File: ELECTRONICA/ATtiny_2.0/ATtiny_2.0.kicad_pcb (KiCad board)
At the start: 2 copper layers, 77.4 x 127.8 mm, 148 parts, among them J1 Puerto_Temperatura_1, J10 Agujero2, J11 Agujero3, J12 Agujero4, J13 GND, J14 VCC, J15 XT30, J2 Puerto_Temperatura_2, J3 I2C0, J4 I2C1, J5 Puerto Motores, J6 UART0, J7 Puerto_Encoders, J8 ICSP, J9 Agujero1, SW1 SW_Push, SW2 SW_DIP_x04, U1 ATtiny1634-SU, U2 L7805, Y1 Crystal 16MHz

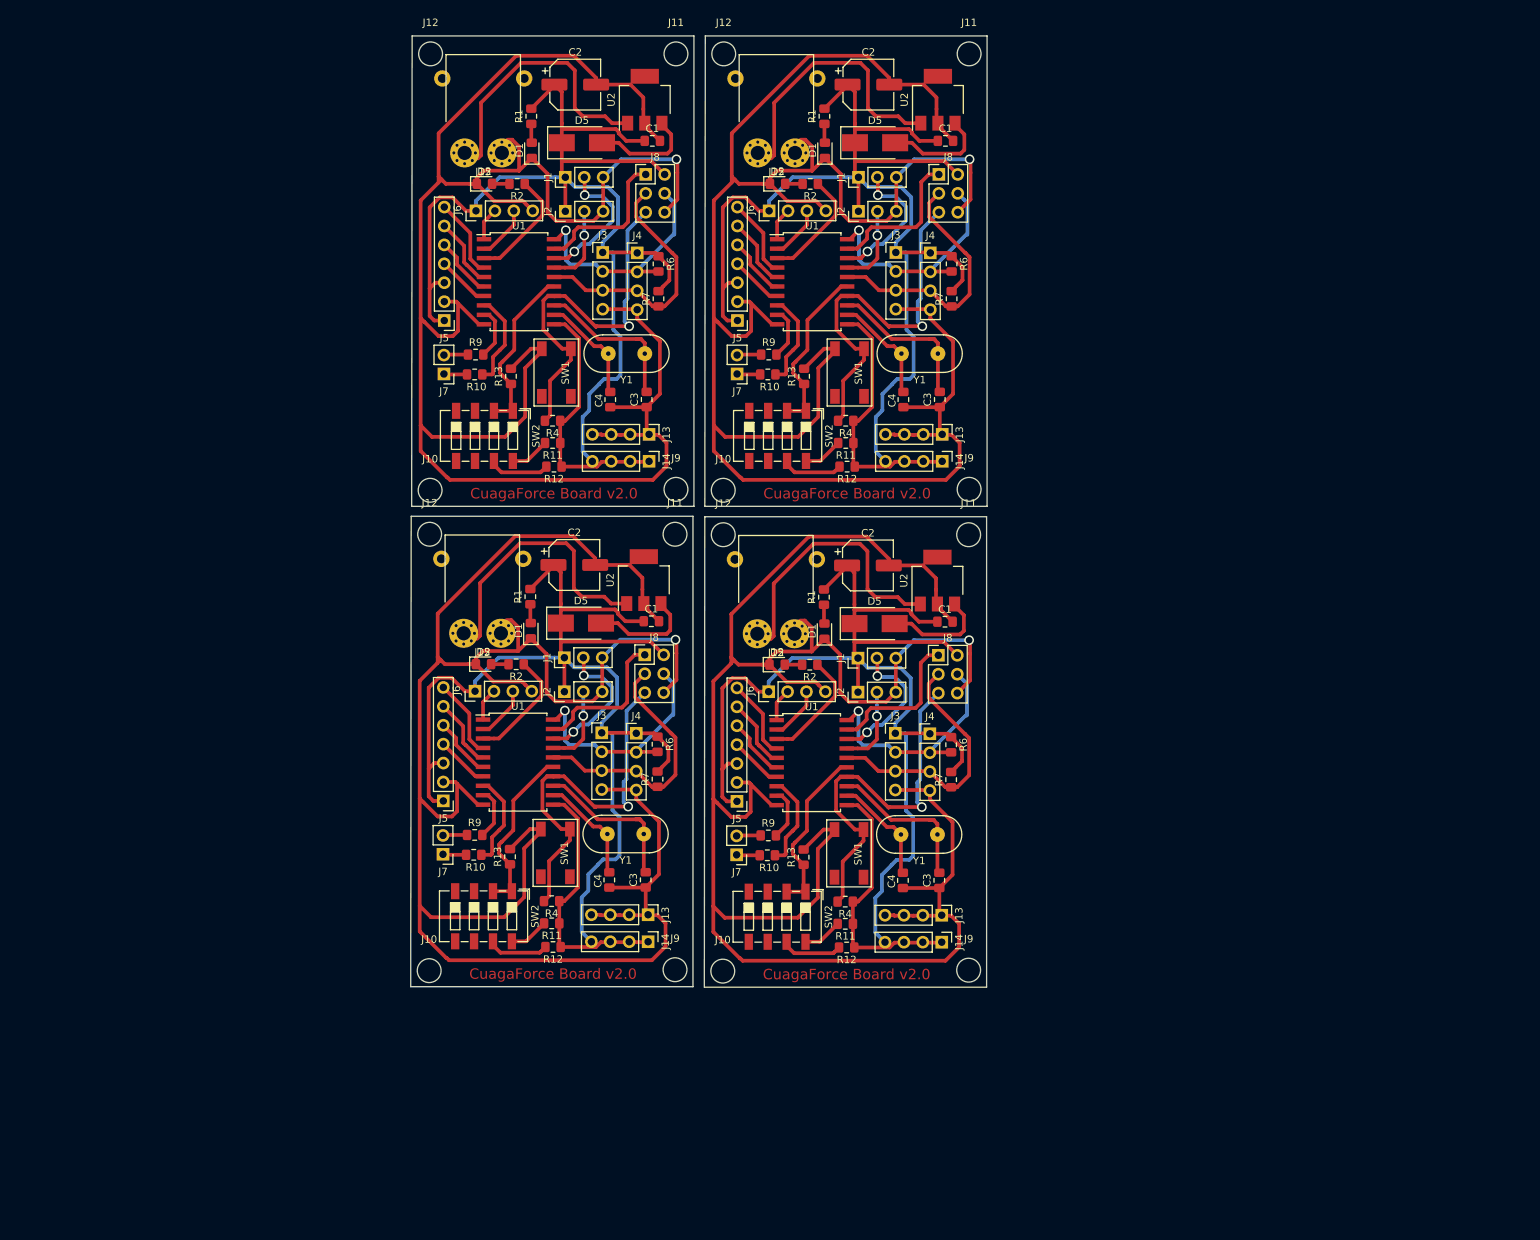
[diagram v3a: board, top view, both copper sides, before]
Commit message: controller reader and controller tanformer to pollotron robot
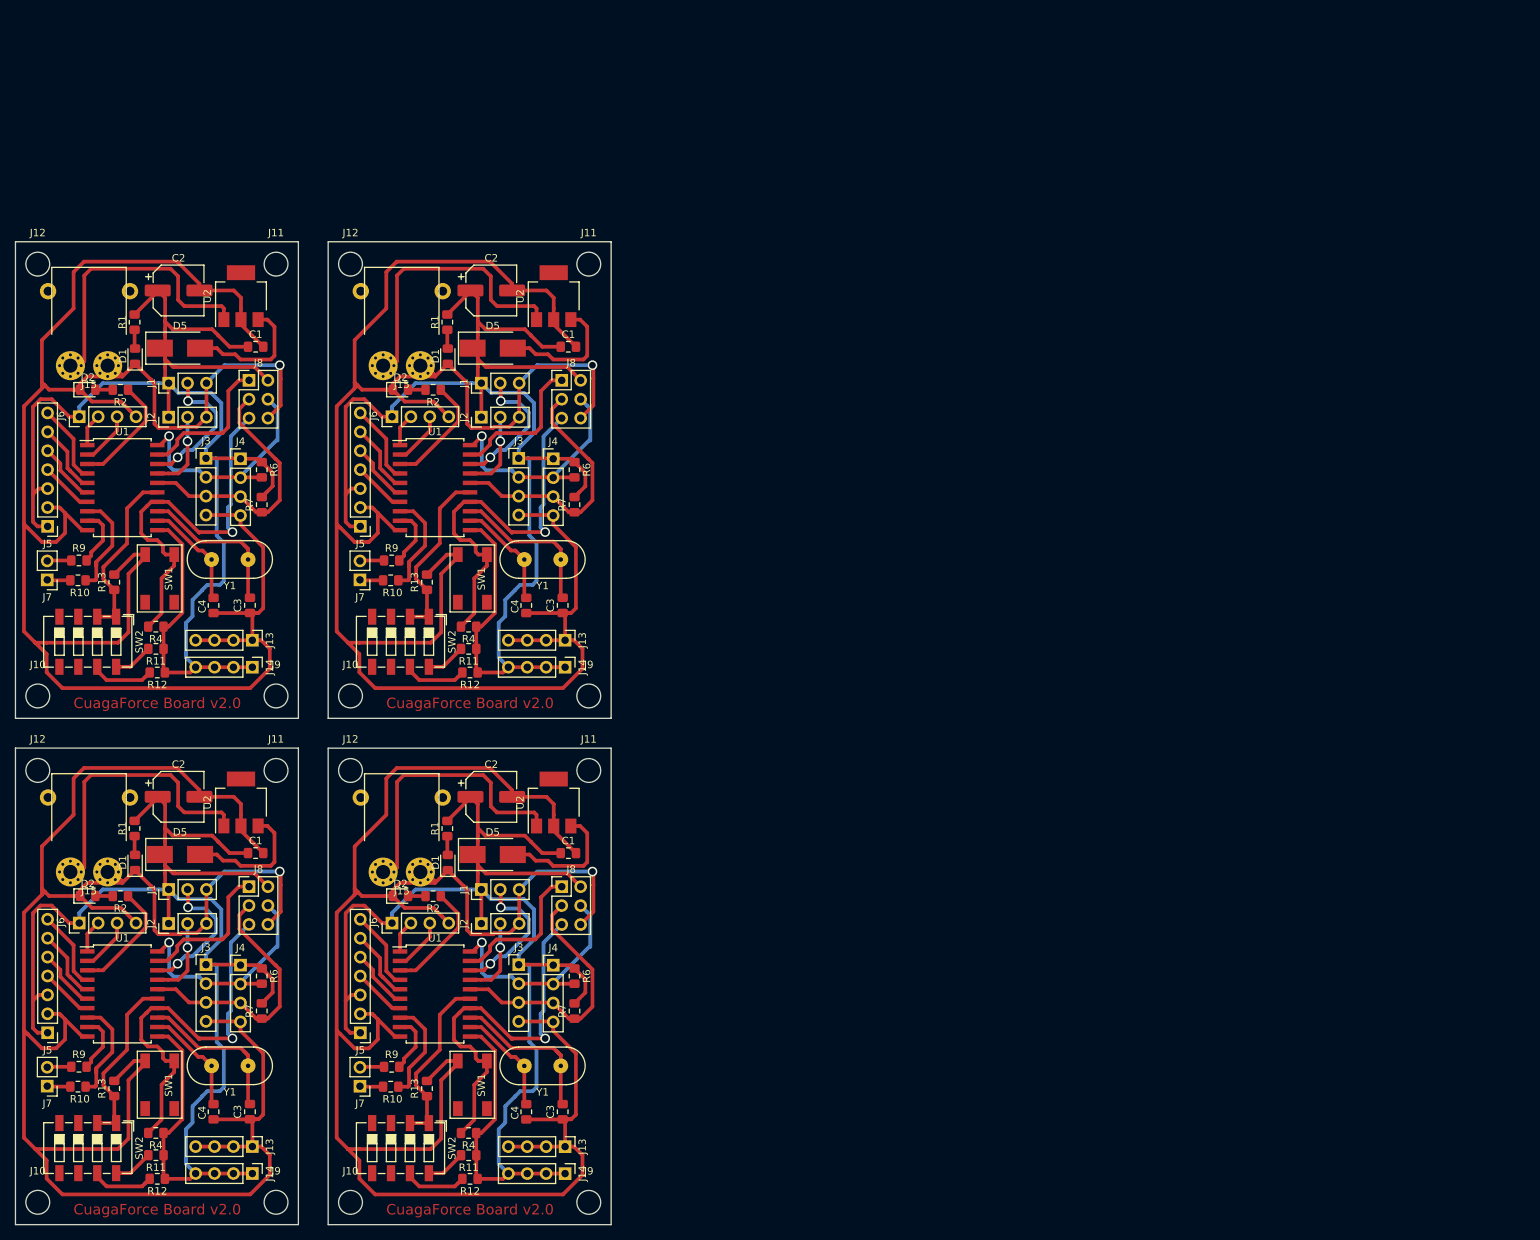
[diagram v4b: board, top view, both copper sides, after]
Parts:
- removed the C1 at (136.8, 89.0)
- removed the C1 at (97.4, 89.0)
- removed the C1 at (136.9, 24.4)
- removed the C2 at (126.5, 81.5)
- removed the C2 at (87.1, 81.4)
- removed the C2 at (126.6, 16.9)
- removed the C3 at (136.1, 123.8)
- removed the C3 at (96.6, 123.7)
- removed the C3 at (136.1, 59.2)
- removed the C4 at (131.2, 123.8)
- removed the C4 at (91.8, 123.7)
- removed the C4 at (131.3, 59.2)
- removed the D1 at (120.7, 90.3)
- removed the D1 at (81.2, 90.2)
- removed the D1 at (120.7, 25.7)
- removed the D2 at (114.3, 94.8)
- removed the D2 at (74.9, 94.7)
- removed the D2 at (114.4, 30.2)
- removed the D5 at (127.4, 89.3)
- removed the D5 at (87.9, 89.2)
- removed the D5 at (127.4, 24.7)
- removed the J1 at (125.2, 93.9)
- removed the J1 at (85.7, 93.9)
- removed the J1 at (125.2, 29.3)
- removed the J10 at (107.0, 136.0)
- removed the J10 at (67.6, 135.9)
- removed the J10 at (107.1, 71.4)
- removed the J11 at (140.0, 77.3)
- removed the J11 at (100.6, 77.3)
- removed the J11 at (140.1, 12.8)
- removed the J12 at (107.1, 77.3)
- removed the J12 at (67.6, 77.3)
- removed the J12 at (107.1, 12.8)
- removed the J13 at (136.4, 128.4)
- removed the J13 at (97.0, 128.4)
- removed the J13 at (136.5, 63.9)
- removed the J14 at (136.4, 132.1)
- removed the J14 at (97.0, 132.0)
- removed the J14 at (136.5, 67.5)
- removed the J15 at (114.1, 90.6)
- removed the J15 at (74.7, 90.6)
- removed the J15 at (114.2, 26.1)
- removed the J2 at (125.2, 98.5)
- removed the J2 at (85.7, 98.4)
- removed the J2 at (125.2, 33.9)
- removed the J3 at (130.2, 104.0)
- removed the J3 at (90.7, 103.9)
- removed the J3 at (130.2, 39.4)
- removed the J4 at (134.8, 104.1)
- removed the J4 at (95.4, 104.0)
- removed the J4 at (134.9, 39.5)
- removed the J5 at (108.9, 113.2)
- removed the J5 at (69.5, 113.1)
- removed the J5 at (109.0, 48.6)
- removed the J6 at (113.2, 98.4)
- removed the J6 at (73.7, 98.4)
- removed the J6 at (113.2, 33.8)
- removed the J7 at (108.9, 120.3)
- removed the J7 at (69.4, 120.3)
- removed the J7 at (108.9, 55.8)
- removed the J8 at (136.0, 93.5)
- removed the J8 at (96.5, 93.5)
- removed the J8 at (136.0, 29.0)
- removed the J9 at (140.0, 135.8)
- removed the J9 at (100.6, 135.8)
- removed the J9 at (140.1, 71.2)
- removed the R1 at (120.6, 85.7)
- removed the R1 at (81.2, 85.7)
- removed the R1 at (120.7, 21.1)
- removed the R10 at (113.0, 120.4)
- removed the R10 at (73.5, 120.3)
- removed the R10 at (113.0, 55.8)
- removed the R11 at (123.5, 129.6)
- removed the R11 at (84.0, 129.5)
- removed the R11 at (123.5, 65.0)
- removed the R12 at (123.6, 132.8)
- removed the R12 at (84.2, 132.7)
- removed the R12 at (123.7, 68.2)
- removed the R13 at (117.9, 120.7)
- removed the R13 at (78.4, 120.6)
- removed the R13 at (117.9, 56.1)
- removed the R2 at (118.7, 94.8)
- removed the R2 at (79.2, 94.7)
- removed the R2 at (118.7, 30.2)
- removed the R4 at (123.4, 126.6)
- removed the R4 at (84.0, 126.6)
- removed the R4 at (123.5, 62.0)
- removed the R6 at (137.7, 105.5)
- removed the R6 at (98.2, 105.5)
- removed the R6 at (137.7, 41.0)
- removed the R7 at (137.7, 110.2)
- removed the R7 at (98.2, 110.2)
- removed the R7 at (137.7, 45.7)
- removed the R9 at (113.1, 117.7)
- removed the R9 at (73.7, 117.7)
- removed the R9 at (113.2, 53.2)
- removed the SW1 at (124.0, 120.1)
- removed the SW1 at (84.5, 120.1)
- removed the SW1 at (124.0, 55.6)
- removed the SW2 at (114.3, 128.7)
- removed the SW2 at (74.9, 128.6)
- removed the SW2 at (114.4, 64.1)
- removed the U1 at (118.9, 108.0)
- removed the U1 at (79.5, 107.9)
- removed the U1 at (119.0, 43.4)
- removed the U2 at (135.8, 83.5)
- removed the U2 at (96.4, 83.4)
- removed the U2 at (135.9, 18.9)
- removed the Y1 at (135.8, 117.6)
- removed the Y1 at (96.4, 117.5)
- removed the Y1 at (135.9, 53.0)
- added C1: C100nF, Capacitor_SMD:C_0805_2012Metric_Pad1.15x1.40mm_HandSolder, F.Cu at (86.3, 120.1)
- added C1: C100nF, Capacitor_SMD:C_0805_2012Metric_Pad1.15x1.40mm_HandSolder, F.Cu at (44.3, 120.1)
- added C1: C100nF, Capacitor_SMD:C_0805_2012Metric_Pad1.15x1.40mm_HandSolder, F.Cu at (86.3, 52.1)
- added C2: CP47uF, Capacitor_SMD:CP_Elec_6.3x5.3, F.Cu at (75.9, 112.5)
- added C2: CP47uF, Capacitor_SMD:CP_Elec_6.3x5.3, F.Cu at (33.9, 112.5)
- added C2: CP47uF, Capacitor_SMD:CP_Elec_6.3x5.3, F.Cu at (75.9, 44.5)
- added C3: C22pF, Capacitor_SMD:C_0805_2012Metric_Pad1.15x1.40mm_HandSolder, F.Cu at (85.5, 154.8)
- added C3: C22pF, Capacitor_SMD:C_0805_2012Metric_Pad1.15x1.40mm_HandSolder, F.Cu at (43.5, 154.8)
- added C3: C22pF, Capacitor_SMD:C_0805_2012Metric_Pad1.15x1.40mm_HandSolder, F.Cu at (85.5, 86.8)
- added C4: C22pF, Capacitor_SMD:C_0805_2012Metric_Pad1.15x1.40mm_HandSolder, F.Cu at (80.6, 154.8)
- added C4: C22pF, Capacitor_SMD:C_0805_2012Metric_Pad1.15x1.40mm_HandSolder, F.Cu at (38.6, 154.8)
- added C4: C22pF, Capacitor_SMD:C_0805_2012Metric_Pad1.15x1.40mm_HandSolder, F.Cu at (80.6, 86.8)
- added D1: LED, LED_SMD:LED_0805_2012Metric_Pad1.15x1.40mm_HandSolder, F.Cu at (70.1, 121.4)
- added D1: LED, LED_SMD:LED_0805_2012Metric_Pad1.15x1.40mm_HandSolder, F.Cu at (28.1, 121.4)
- added D1: LED, LED_SMD:LED_0805_2012Metric_Pad1.15x1.40mm_HandSolder, F.Cu at (70.1, 53.4)
- added D2: LED, LED_SMD:LED_0805_2012Metric_Pad1.15x1.40mm_HandSolder, F.Cu at (63.7, 125.9)
- added D2: LED, LED_SMD:LED_0805_2012Metric_Pad1.15x1.40mm_HandSolder, F.Cu at (21.7, 125.9)
- added D2: LED, LED_SMD:LED_0805_2012Metric_Pad1.15x1.40mm_HandSolder, F.Cu at (63.7, 57.9)
- added D5: US2D, Diode_SMD:D_SMB_Handsoldering, F.Cu at (76.1, 120.3)
- added D5: US2D, Diode_SMD:D_SMB_Handsoldering, F.Cu at (34.1, 120.3)
- added D5: US2D, Diode_SMD:D_SMB_Handsoldering, F.Cu at (76.1, 52.3)
- added J1: Puerto_Temperatura_1, Connector_PinHeader_2.54mm:PinHeader_1x03_P2.54mm_Vertical, F.Cu at (74.6, 125.0)
- added J1: Puerto_Temperatura_1, Connector_PinHeader_2.54mm:PinHeader_1x03_P2.54mm_Vertical, F.Cu at (32.6, 125.0)
- added J1: Puerto_Temperatura_1, Connector_PinHeader_2.54mm:PinHeader_1x03_P2.54mm_Vertical, F.Cu at (74.6, 57.0)
- added J10: Agujero2, MountingHole:MountingHole_3.2mm_M3, F.Cu at (57.0, 167.0)
- added J10: Agujero2, MountingHole:MountingHole_3.2mm_M3, F.Cu at (15.0, 167.0)
- added J10: Agujero2, MountingHole:MountingHole_3.2mm_M3, F.Cu at (57.0, 99.0)
- added J11: Agujero3, MountingHole:MountingHole_3.2mm_M3, F.Cu at (89.0, 109.0)
- added J11: Agujero3, MountingHole:MountingHole_3.2mm_M3, F.Cu at (47.0, 109.0)
- added J11: Agujero3, MountingHole:MountingHole_3.2mm_M3, F.Cu at (89.0, 41.0)
- added J12: Agujero4, MountingHole:MountingHole_3.2mm_M3, F.Cu at (57.0, 109.0)
- added J12: Agujero4, MountingHole:MountingHole_3.2mm_M3, F.Cu at (15.0, 109.0)
- added J12: Agujero4, MountingHole:MountingHole_3.2mm_M3, F.Cu at (57.0, 41.0)
- added J13: GND, Connector_PinHeader_2.54mm:PinHeader_1x04_P2.54mm_Vertical, F.Cu at (85.8, 159.5)
- added J13: GND, Connector_PinHeader_2.54mm:PinHeader_1x04_P2.54mm_Vertical, F.Cu at (43.8, 159.5)
- added J13: GND, Connector_PinHeader_2.54mm:PinHeader_1x04_P2.54mm_Vertical, F.Cu at (85.8, 91.5)
- added J14: VCC, Connector_PinHeader_2.54mm:PinHeader_1x04_P2.54mm_Vertical, F.Cu at (85.8, 163.1)
- added J14: VCC, Connector_PinHeader_2.54mm:PinHeader_1x04_P2.54mm_Vertical, F.Cu at (43.8, 163.1)
- added J14: VCC, Connector_PinHeader_2.54mm:PinHeader_1x04_P2.54mm_Vertical, F.Cu at (85.8, 95.1)
- added J15: XT30, proyectoAjeno:XT30PW-F, F.Cu at (63.9, 122.6)
- added J15: XT30, proyectoAjeno:XT30PW-F, F.Cu at (21.9, 122.6)
- added J15: XT30, proyectoAjeno:XT30PW-F, F.Cu at (63.9, 54.6)
- added J2: Puerto_Temperatura_2, Connector_PinHeader_2.54mm:PinHeader_1x03_P2.54mm_Vertical, F.Cu at (74.6, 129.6)
- added J2: Puerto_Temperatura_2, Connector_PinHeader_2.54mm:PinHeader_1x03_P2.54mm_Vertical, F.Cu at (32.6, 129.6)
- added J2: Puerto_Temperatura_2, Connector_PinHeader_2.54mm:PinHeader_1x03_P2.54mm_Vertical, F.Cu at (74.6, 61.6)
- added J3: I2C0, Connector_PinHeader_2.54mm:PinHeader_1x04_P2.54mm_Vertical, F.Cu at (79.6, 135.1)
- added J3: I2C0, Connector_PinHeader_2.54mm:PinHeader_1x04_P2.54mm_Vertical, F.Cu at (37.6, 135.1)
- added J3: I2C0, Connector_PinHeader_2.54mm:PinHeader_1x04_P2.54mm_Vertical, F.Cu at (79.6, 67.1)
- added J4: I2C1, Connector_PinHeader_2.54mm:PinHeader_1x04_P2.54mm_Vertical, F.Cu at (84.2, 135.2)
- added J4: I2C1, Connector_PinHeader_2.54mm:PinHeader_1x04_P2.54mm_Vertical, F.Cu at (42.2, 135.1)
- added J4: I2C1, Connector_PinHeader_2.54mm:PinHeader_1x04_P2.54mm_Vertical, F.Cu at (84.2, 67.1)
- added J5: Puerto Motores, Connector_PinHeader_2.54mm:PinHeader_1x07_P2.54mm_Vertical, F.Cu at (58.3, 144.2)
- added J5: Puerto Motores, Connector_PinHeader_2.54mm:PinHeader_1x07_P2.54mm_Vertical, F.Cu at (16.3, 144.2)
- added J5: Puerto Motores, Connector_PinHeader_2.54mm:PinHeader_1x07_P2.54mm_Vertical, F.Cu at (58.3, 76.2)
- added J6: UART0, Connector_PinHeader_2.54mm:PinHeader_1x04_P2.54mm_Vertical, F.Cu at (62.6, 129.5)
- added J6: UART0, Connector_PinHeader_2.54mm:PinHeader_1x04_P2.54mm_Vertical, F.Cu at (20.6, 129.5)
- added J6: UART0, Connector_PinHeader_2.54mm:PinHeader_1x04_P2.54mm_Vertical, F.Cu at (62.6, 61.5)
- added J7: Puerto_Encoders, Connector_PinHeader_2.54mm:PinHeader_1x02_P2.54mm_Vertical, F.Cu at (58.3, 151.4)
- added J7: Puerto_Encoders, Connector_PinHeader_2.54mm:PinHeader_1x02_P2.54mm_Vertical, F.Cu at (16.3, 151.4)
- added J7: Puerto_Encoders, Connector_PinHeader_2.54mm:PinHeader_1x02_P2.54mm_Vertical, F.Cu at (58.3, 83.4)
- added J8: ICSP, Connector_PinHeader_2.54mm:PinHeader_2x03_P2.54mm_Vertical, F.Cu at (85.4, 124.6)
- added J8: ICSP, Connector_PinHeader_2.54mm:PinHeader_2x03_P2.54mm_Vertical, F.Cu at (43.4, 124.6)
- added J8: ICSP, Connector_PinHeader_2.54mm:PinHeader_2x03_P2.54mm_Vertical, F.Cu at (85.4, 56.6)
- added J9: Agujero1, MountingHole:MountingHole_3.2mm_M3, F.Cu at (89.0, 167.0)
- added J9: Agujero1, MountingHole:MountingHole_3.2mm_M3, F.Cu at (47.0, 167.0)
- added J9: Agujero1, MountingHole:MountingHole_3.2mm_M3, F.Cu at (89.0, 99.0)
- added R1: R330, Resistor_SMD:R_0805_2012Metric_Pad1.15x1.40mm_HandSolder, F.Cu at (70.0, 116.8)
- added R1: R330, Resistor_SMD:R_0805_2012Metric_Pad1.15x1.40mm_HandSolder, F.Cu at (28.0, 116.8)
- added R1: R330, Resistor_SMD:R_0805_2012Metric_Pad1.15x1.40mm_HandSolder, F.Cu at (70.0, 48.8)
- added R10: R10K, Resistor_SMD:R_0805_2012Metric_Pad1.15x1.40mm_HandSolder, F.Cu at (62.4, 151.5)
- added R10: R10K, Resistor_SMD:R_0805_2012Metric_Pad1.15x1.40mm_HandSolder, F.Cu at (20.4, 151.5)
- added R10: R10K, Resistor_SMD:R_0805_2012Metric_Pad1.15x1.40mm_HandSolder, F.Cu at (62.4, 83.5)
- added R11: R1K, Resistor_SMD:R_0805_2012Metric_Pad1.15x1.40mm_HandSolder, F.Cu at (72.9, 160.7)
- added R11: R1K, Resistor_SMD:R_0805_2012Metric_Pad1.15x1.40mm_HandSolder, F.Cu at (30.9, 160.7)
- added R11: R1K, Resistor_SMD:R_0805_2012Metric_Pad1.15x1.40mm_HandSolder, F.Cu at (72.9, 92.7)
- added R12: R10K, Resistor_SMD:R_0805_2012Metric_Pad1.15x1.40mm_HandSolder, F.Cu at (73.0, 163.9)
- added R12: R10K, Resistor_SMD:R_0805_2012Metric_Pad1.15x1.40mm_HandSolder, F.Cu at (31.1, 163.8)
- added R12: R10K, Resistor_SMD:R_0805_2012Metric_Pad1.15x1.40mm_HandSolder, F.Cu at (73.0, 95.8)
- added R13: R100K, Resistor_SMD:R_0805_2012Metric_Pad1.15x1.40mm_HandSolder, F.Cu at (67.3, 151.7)
- added R13: R100K, Resistor_SMD:R_0805_2012Metric_Pad1.15x1.40mm_HandSolder, F.Cu at (25.3, 151.7)
- added R13: R100K, Resistor_SMD:R_0805_2012Metric_Pad1.15x1.40mm_HandSolder, F.Cu at (67.3, 83.7)
- added R2: R330, Resistor_SMD:R_0805_2012Metric_Pad1.15x1.40mm_HandSolder, F.Cu at (68.1, 125.9)
- added R2: R330, Resistor_SMD:R_0805_2012Metric_Pad1.15x1.40mm_HandSolder, F.Cu at (26.1, 125.9)
- added R2: R330, Resistor_SMD:R_0805_2012Metric_Pad1.15x1.40mm_HandSolder, F.Cu at (68.1, 57.9)
- added R4: R10K, Resistor_SMD:R_0805_2012Metric_Pad1.15x1.40mm_HandSolder, F.Cu at (72.9, 157.7)
- added R4: R10K, Resistor_SMD:R_0805_2012Metric_Pad1.15x1.40mm_HandSolder, F.Cu at (30.9, 157.7)
- added R4: R10K, Resistor_SMD:R_0805_2012Metric_Pad1.15x1.40mm_HandSolder, F.Cu at (72.9, 89.7)
- added R6: R10K, Resistor_SMD:R_0805_2012Metric_Pad1.15x1.40mm_HandSolder, F.Cu at (87.1, 136.6)
- added R6: R10K, Resistor_SMD:R_0805_2012Metric_Pad1.15x1.40mm_HandSolder, F.Cu at (45.1, 136.6)
- added R6: R10K, Resistor_SMD:R_0805_2012Metric_Pad1.15x1.40mm_HandSolder, F.Cu at (87.1, 68.6)
- added R7: R10K, Resistor_SMD:R_0805_2012Metric_Pad1.15x1.40mm_HandSolder, F.Cu at (87.1, 141.3)
- added R7: R10K, Resistor_SMD:R_0805_2012Metric_Pad1.15x1.40mm_HandSolder, F.Cu at (45.1, 141.3)
- added R7: R10K, Resistor_SMD:R_0805_2012Metric_Pad1.15x1.40mm_HandSolder, F.Cu at (87.1, 73.3)
- added R9: R10K, Resistor_SMD:R_0805_2012Metric_Pad1.15x1.40mm_HandSolder, F.Cu at (62.5, 148.8)
- added R9: R10K, Resistor_SMD:R_0805_2012Metric_Pad1.15x1.40mm_HandSolder, F.Cu at (20.5, 148.8)
- added R9: R10K, Resistor_SMD:R_0805_2012Metric_Pad1.15x1.40mm_HandSolder, F.Cu at (62.5, 80.8)
- added SW1: SW_Push, huellas:Pulsador_5,2x5,2, F.Cu at (73.4, 151.2)
- added SW1: SW_Push, huellas:Pulsador_5,2x5,2, F.Cu at (31.4, 151.2)
- added SW1: SW_Push, huellas:Pulsador_5,2x5,2, F.Cu at (73.4, 83.2)
- added SW2: SW_DIP_x04, Button_Switch_SMD:SW_DIP_SPSTx04_Slide_6.7x11.72mm_W6.73mm_P2.54mm_LowProfile_JPin, F.Cu at (63.7, 159.7)
- added SW2: SW_DIP_x04, Button_Switch_SMD:SW_DIP_SPSTx04_Slide_6.7x11.72mm_W6.73mm_P2.54mm_LowProfile_JPin, F.Cu at (21.7, 159.7)
- added SW2: SW_DIP_x04, Button_Switch_SMD:SW_DIP_SPSTx04_Slide_6.7x11.72mm_W6.73mm_P2.54mm_LowProfile_JPin, F.Cu at (63.7, 91.7)
- added U1: ATtiny1634-SU, Package_SO:SOIC-20W_7.5x12.8mm_P1.27mm, F.Cu at (68.4, 139.0)
- added U1: ATtiny1634-SU, Package_SO:SOIC-20W_7.5x12.8mm_P1.27mm, F.Cu at (26.4, 139.0)
- added U1: ATtiny1634-SU, Package_SO:SOIC-20W_7.5x12.8mm_P1.27mm, F.Cu at (68.4, 71.0)
- added U2: L7805, Package_TO_SOT_SMD:SOT-223, F.Cu at (84.3, 113.3)
- added U2: L7805, Package_TO_SOT_SMD:SOT-223, F.Cu at (42.3, 113.3)
- added U2: L7805, Package_TO_SOT_SMD:SOT-223, F.Cu at (84.3, 45.3)
- added Y1: Crystal 16MHz, Compluino_03:Crystal, F.Cu at (85.2, 148.7)
- added Y1: Crystal 16MHz, Compluino_03:Crystal, F.Cu at (43.2, 148.7)
- added Y1: Crystal 16MHz, Compluino_03:Crystal, F.Cu at (85.2, 80.7)
- moved J11 60.7 mm to (47.0, 41.0)
- moved D5 60.6 mm to (34.1, 52.3)
- moved J9 60.5 mm to (47.0, 99.0)
- moved U2 60.3 mm to (42.3, 45.3)
- moved J15 60.2 mm to (21.9, 54.6)
- moved C2 60.0 mm to (33.9, 44.5)
- moved C4 60.0 mm to (38.6, 86.8)
- moved D1 60.0 mm to (28.1, 53.4)
- moved J1 60.0 mm to (32.6, 57.0)
- moved J2 60.0 mm to (32.6, 61.6)
- moved J4 60.0 mm to (42.2, 67.1)
- moved J5 60.0 mm to (16.3, 76.2)
- moved J7 60.0 mm to (16.3, 83.4)
- moved J8 60.0 mm to (43.4, 56.6)
- moved R1 60.0 mm to (28.0, 48.8)
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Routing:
- net (no net): track 2567.2 -> 2605.3 mm
- net Net-(D5-Pad2): track 14.2 -> 17.3 mm
- net INT2: track 7.04 -> 9.44 mm
- net +5V: track 189.5 -> 191.6 mm
- net INT1: track 12.8 -> 14.4 mm
- net RESET: track 50.1 -> 51.5 mm
- net VPP: track 35.9 -> 36.8 mm
- net Earth: track 280.3 -> 281.0 mm
- net SWITCH: track 23.4 -> 24.1 mm
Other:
- board size 77.4 x 127.8 mm -> 80 x 132 mm
